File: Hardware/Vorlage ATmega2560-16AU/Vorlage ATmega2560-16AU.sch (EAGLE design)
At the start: 151 parts, among them IC1 CD74HC14PW, IC2 ATMEGA2560640V-8AU, IC3 SS39E, IC4 SS39E, IC5 74AC138D, IC6 XC6210B332MR, Q1 16MHz, Q10 PMV27UPER, Q2 32.768kHz, Q3 PMV27UPER, Q4 PMV27UPER, Q5 PMV27UPER, Q6 PMV27UPER, Q7 PMV27UPER, Q8 PMV27UPER, Q9 PMV27UPER, U1 LM35DZ, X1 2510-, X2 +5V, X3 2514-, X4 2510-, X5 2510-

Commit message: Schema neu angeordnet
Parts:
- added C26: 100nF, rcl:C-EUC1206
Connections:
- net N$32 renamed PC0
- net N$35 renamed PC1
- net N$36 renamed PC2
- net N$38 renamed PC3
- net N$41 renamed PC4
- net N$42 renamed PC5
- net N$45 renamed PA0
- net N$54 renamed PH5
- net N$62 renamed PH4
- net N$71 renamed PA1
- net N$72 renamed PA2
- net N$73 renamed PH3
- net N$74 renamed PA3
- net N$76 renamed PA4
- net N$77 renamed PA5
- net N$78 renamed PA6
- net N$79 renamed PA7
- net N$80 renamed PB0
- net N$81 renamed PB1
- net N$82 renamed PB2
- net N$83 renamed PB3
- net N$84 renamed PB4
- net N$85 renamed PB5
- net N$86 renamed PB6
- net N$87 renamed PB7
- removed net N$43: IC2.(A14)PC6, S11.P
- removed net N$44: IC2.(A15)PC7, S12.P
- new net N$32: C17.1, IC2.(TOSC1)PG4, Q2.1
- new net N$35: C18.1, IC2.(ALE)PG2, Q2.2
- net GND: now also C26.2, IC5P.GND
- net PC6: now also IC2.(A14)PC6, S11.P; no longer C18.1, IC2.(TOSC2)PG3, Q2.2
- net PC7: now also IC2.(A15)PC7, S12.P; no longer C17.1, IC2.(TOSC1)PG4, Q2.1
- net VCC: now also C26.1, IC5P.VCC
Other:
- note added: "LEDs"
- note added: "LEDs 0...7 (PA0 = LED0)"
- note added: "RGB-LED"
- note added: "Schalter"
- note added: "X5 und LEDs 8...15 (PB0 = LED8)"
- moved on the sheet: +5V-POWER, 3.3V, C1, C10, C11, C14, C15, C16, C19, C2, C20, C21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

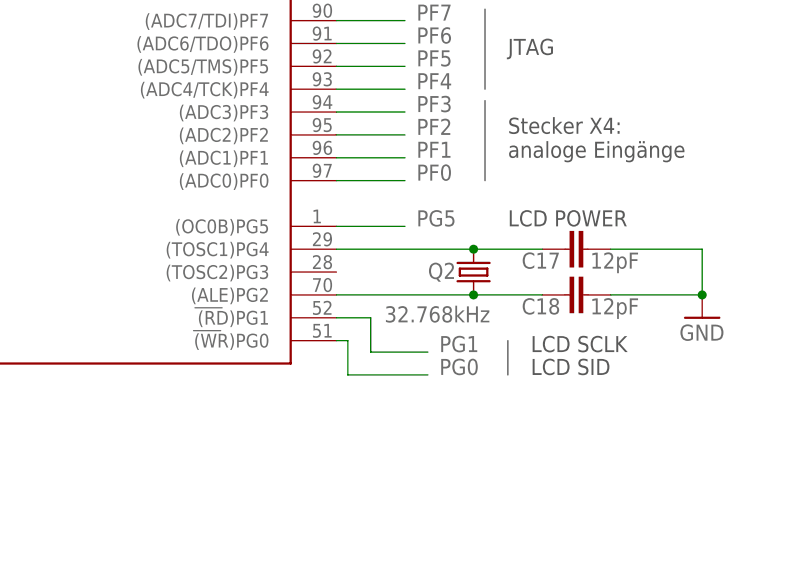
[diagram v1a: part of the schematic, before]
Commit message: Quarz Q2 richtig verbunden
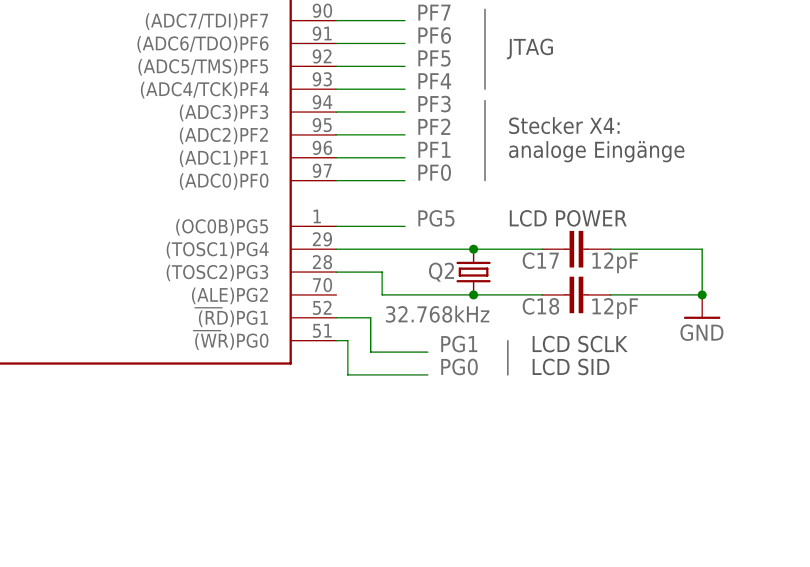
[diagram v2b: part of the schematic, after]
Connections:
- net N$35: now also IC2.(TOSC2)PG3; no longer IC2.(ALE)PG2
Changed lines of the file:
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@@
 <pinref part="Q2" gate="G$1" pin="2"/>
 <wire x1="226.06" y1="180.34" x2="218.44" y2="180.34" width="0.1524" layer="91"/>
-<pinref part="IC2" gate="1" pin="(ALE)PG2"/>
-<wire x1="218.44" y1="180.34" x2="203.2" y2="180.34" width="0.1524" layer="91"/>
+<pinref part="IC2" gate="1" pin="(TOSC2)PG3"/>
+<wire x1="203.2" y1="182.88" x2="208.28" y2="182.88" width="0.1524" layer="91"/>
+<wire x1="208.28" y1="182.88" x2="208.28" y2="180.34" width="0.1524" layer="91"/>
+<wire x1="208.28" y1="180.34" x2="218.44" y2="180.34" width="0.1524" layer="91"/>
 <junction x="218.44" y="180.34"/>
 </segment>
